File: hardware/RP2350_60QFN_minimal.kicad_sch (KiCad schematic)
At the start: 39 parts, among them J4 SM03B-SRSS-TB, J5 4677, SW1 SW_Push, SW2 SW_Push, U1 RP2350_60QFN, U3 W25Q128JVS, Y1 ABM8-272-T3

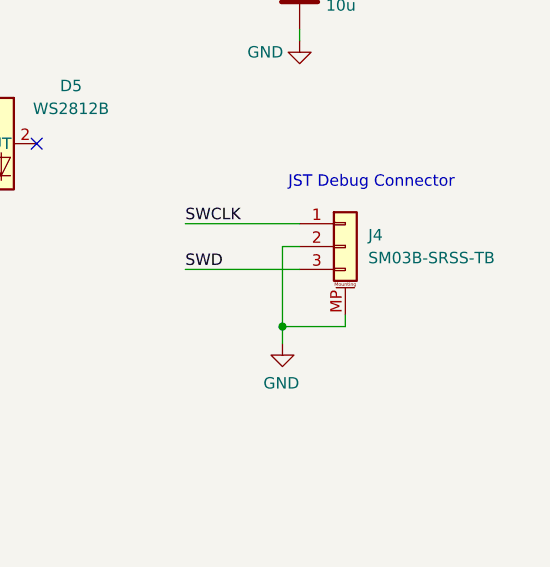
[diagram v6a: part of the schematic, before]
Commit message: feat(hardware): Add test point connections + update PCB layout
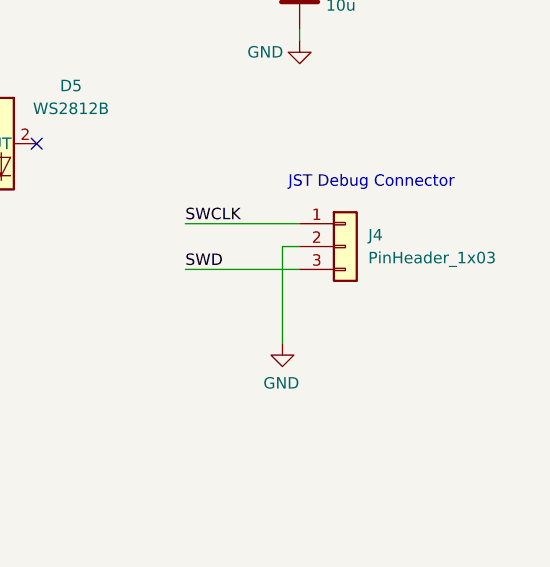
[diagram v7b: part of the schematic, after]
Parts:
- J4: value SM03B-SRSS-TB -> PinHeader_1x03; footprint Connector_JST:JST_SH_SM03B-SRSS-TB_1x03-1MP_P1.00mm_Horizontal -> Connector_PinHeader_2.54mm:PinHeader_1x03_P2.54mm_Vertical; symbol Connector_Generic_MountingPin:Conn_01x03_MountingPin -> Connector_Generic:Conn_01x03
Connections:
- net GND: no longer J4.MP (MountPin)
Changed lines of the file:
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@@
 	)
 	(junction
-		(at 354.965 176.53)
-		(diameter 0)
-		(color 0 0 0 0)
-	)
-	(junction
 		(at 292.1 80.01)
 		(diameter 0)
@@
 	(wire
 		(pts
-			(xy 354.965 167.64) (xy 354.965 176.53)
+			(xy 354.965 167.64) (xy 354.965 178.435)
 		)
 		(stroke
@@
 	(wire
 		(pts
-			(xy 361.95 175.26) (xy 361.95 176.53)
-		)
-		(stroke
-			(width 0)
-			(type default)
-		)
-	)
-	(wire
-		(pts
 			(xy 204.47 129.54) (xy 180.34 129.54)
 		)
@@
 	(wire
 		(pts
-			(xy 354.965 176.53) (xy 361.95 176.53)
-		)
-		(stroke
-			(width 0)
-			(type default)
-		)
-	)
-	(wire
-		(pts
 			(xy 287.02 114.3) (xy 300.99 114.3)
 		)
@@
 	(wire
 		(pts
-			(xy 354.965 176.53) (xy 354.965 178.435)
-		)
-		(stroke
-			(width 0)
-			(type default)
-		)
-	)
-	(wire
-		(pts
 			(xy 326.39 81.28) (xy 326.39 80.01)
 		)
@@
 	)
 	(symbol
-		(lib_id "Connector_Generic_MountingPin:Conn_01x03_MountingPin")
+		(lib_id "Connector_Generic:Conn_01x03")
 		(at 361.95 167.64 0)
 		(unit 1)
@@
 		(fields_autoplaced yes)
 		(property "Reference" "J4"
-			(at 364.49 166.37 0)
+			(at 364.49 166.3699 0)
 			(effects
 				(font
@@
 			)
 		)
-		(property "Value" "SM03B-SRSS-TB"
-			(at 364.49 168.91 0)
+		(property "Value" "PinHeader_1x03"
+			(at 364.49 168.9099 0)
 			(effects
 				(font
@@
 			)
 		)
-		(property "Footprint" "Connector_JST:JST_SH_SM03B-SRSS-TB_1x03-1MP_P1.00mm_Horizontal"
+		(property "Footprint" "Connector_PinHeader_2.54mm:PinHeader_1x03_P2.54mm_Vertical"
 			(at 361.95 167.64 0)
 			(effects
@@
 			)
 		)
-		(property "Description" ""
+		(property "Description" "Generic connector, single row, 01x03, script generated (kicad-library-utils/schlib/autogen/connector/)"
 			(at 361.95 167.64 0)
 			(effects
@@
 					(size 1.27 1.27)
 				)
+				(hide yes)
 			)
 		)
@@
 		(pin "3"
 		)
-		(pin "MP"
-		)
 		(instances

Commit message: feat(hardware): Update switch footprint
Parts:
- SW1, SW2: footprint Button_Switch_SMD:SW_Push_1P1T_NO_Vertical_Wuerth_434133025816 -> TL3365AF180QG:SW_TL3365AF180QG; Purchase Link (none) -> https://www.digikey.com/en/products/detail/e-switch/TL3365A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
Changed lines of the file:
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@@
 			)
 		)
-		(property "Footprint" "Button_Switch_SMD:SW_Push_1P1T_NO_Vertical_Wuerth_434133025816"
+		(property "Footprint" "TL3365AF180QG:SW_TL3365AF180QG"
 			(at 171.45 179.07 0)
 			(effects
@@
 			)
 		)
-		(property "Purchase Link" ""
+		(property "Purchase Link" "https://www.digikey.com/en/products/detail/e-switch/TL3365AF180QG/5964411"
 			(at 171.45 184.15 0)
 			(effects
@@
 			)
 		)
-		(property "Footprint" "Button_Switch_SMD:SW_Push_1P1T_NO_Vertical_Wuerth_434133025816"
+		(property "Footprint" "TL3365AF180QG:SW_TL3365AF180QG"
 			(at 160.655 149.86 0)
 			(effects
@@
 			)
 		)
-		(property "Purchase Link" ""
+		(property "Purchase Link" "https://www.digikey.com/en/products/detail/e-switch/TL3365AF180QG/5964411"
 			(at 165.735 149.86 90)
 			(effects
